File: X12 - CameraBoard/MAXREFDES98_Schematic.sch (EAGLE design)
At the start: 24 parts, among them U1 MB110S-TP, U2 MB110S-TP, U3 MAX5969AETB+, U4 MAX17503ATP+

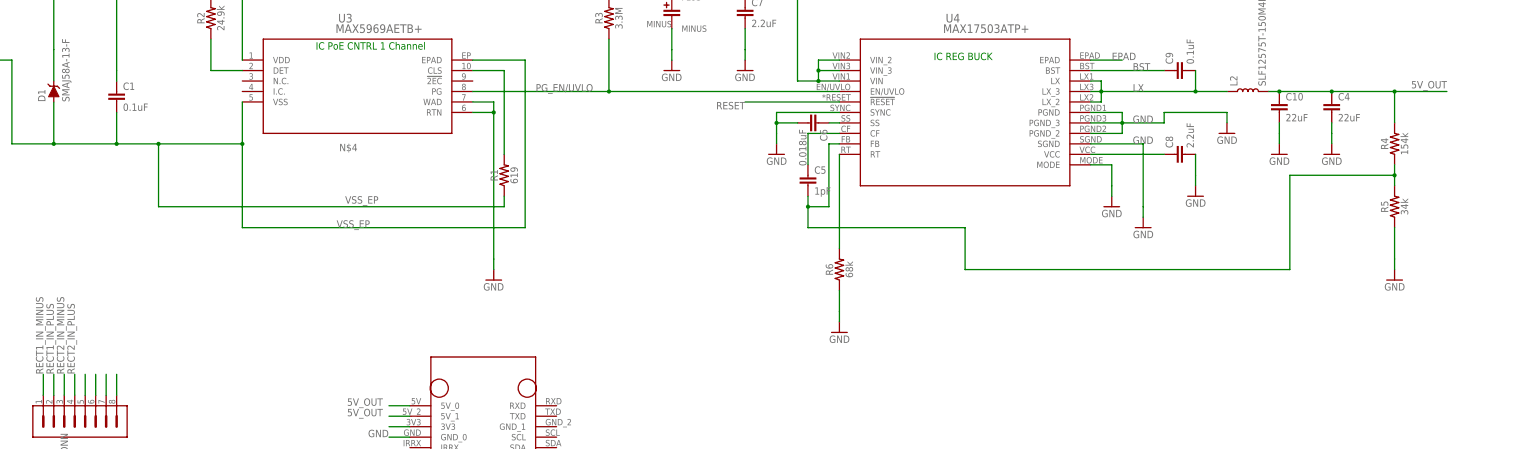
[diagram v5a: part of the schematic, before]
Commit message: Added 0 Ohm Resistor amd 1-pin connector directly to 5V line
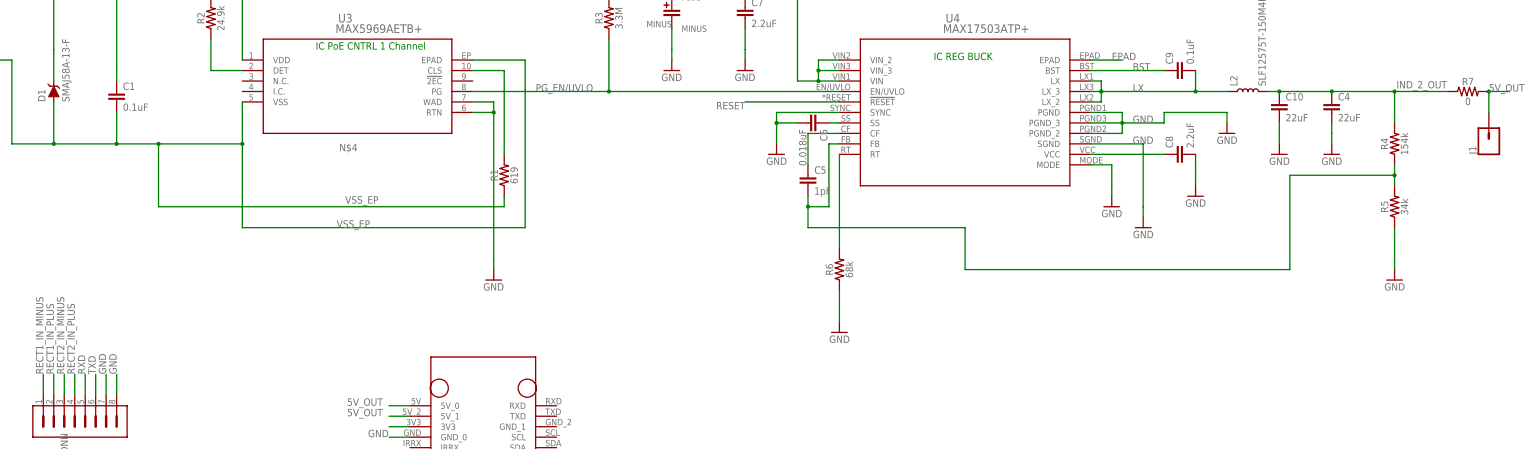
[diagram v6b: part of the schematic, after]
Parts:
- added J1: (no value), SparkFun-Connectors:CONN_01
- added R7: 0, SparkFun-Resistors:0OHM-0603-1/10W-5%
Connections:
- net 5V_OUT5 renamed RXD
- new net IND_2_OUT: C10.1, C4.1, L2.2, R4.2, R7.1
- new net TXD: CONN.6
- net 5V_OUT: now also J1.1, R7.2; no longer C10.1, C4.1, CONN.6, L2.2, R4.2
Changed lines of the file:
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@@
 <part name="CONN" library="Camera_Board_Parts_09_30_2020" deviceset="TERM_BLOCK_PLUG_8POS_STR_2.5MM" device=""/>
 <part name="U$2" library="Camera_Board_Parts_09_30_2020" deviceset="NANO_PI" device=""/>
+<part name="R7" library="SparkFun-Resistors" library_urn="urn:adsk.eagle:library:532" deviceset="0OHM" device="-0603-1/10W-5%" package3d_urn="urn:adsk.eagle:package:39650/1" value="0"/>
+<part name="J1" library="SparkFun-Connectors" library_urn="urn:adsk.eagle:library:513" deviceset="CONN_01" device="" package3d_urn="urn:adsk.eagle:package:38028/1"/>
 </parts>
 <sheets>
@@
 </instance>
 <instance part="U$2" gate="G$1" x="20.32" y="-119.38" smashed="yes"/>
+<instance part="R7" gate="G$1" x="271.78" y="0" smashed="yes">
+<attribute name="NAME" x="271.78" y="1.524" size="1.778" layer="95" font="vector" align="bottom-center"/>
+<attribute name="VALUE" x="271.78" y="-1.524" size="1.778" layer="96" font="vector" align="top-center"/>
+</instance>
+<instance part="J1" gate="G$1" x="276.86" y="-12.7" smashed="yes" rot="R90">
+<attribute name="VALUE" x="281.686" y="-15.24" size="1.778" layer="96" font="vector" rot="R90"/>
+<attribute name="NAME" x="273.812" y="-15.24" size="1.778" layer="95" font="vector" rot="R90"/>
+</instance>
 </instances>
 <busses>
@@
 <net name="5V_OUT" class="0">
 <segment>
-<pinref part="C4" gate="G$1" pin="1"/>
-<pinref part="C10" gate="G$1" pin="1"/>
-<wire x1="226.06" y1="0" x2="238.76" y2="0" width="0.1524" layer="91"/>
-<junction x="226.06" y="0"/>
-<pinref part="L2" gate="G$1" pin="2"/>
-<wire x1="223.52" y1="0" x2="226.06" y2="0" width="0.1524" layer="91"/>
-<pinref part="R4" gate="G$1" pin="2"/>
-<wire x1="238.76" y1="0" x2="254" y2="0" width="0.1524" layer="91"/>
-<wire x1="254" y1="0" x2="254" y2="-7.62" width="0.1524" layer="91"/>
-<junction x="238.76" y="0"/>
-<wire x1="254" y1="0" x2="266.7" y2="0" width="0.1524" layer="91"/>
-<junction x="254" y="0"/>
-<label x="266.7" y="2.54" size="1.778" layer="95" rot="R180"/>
-</segment>
-<segment>
-<pinref part="CONN" gate="G$1" pin="6"/>
-<wire x1="-60.96" y1="-73.66" x2="-60.96" y2="-68.58" width="0.1524" layer="91"/>
-</segment>
-<segment>
 <pinref part="U$2" gate="G$1" pin="5V_0"/>
 <wire x1="15.24" y1="-76.2" x2="10.16" y2="-76.2" width="0.1524" layer="91"/>
@@
 <wire x1="15.24" y1="-78.74" x2="10.16" y2="-78.74" width="0.1524" layer="91"/>
 <label x="0" y="-78.74" size="1.778" layer="95"/>
+</segment>
+<segment>
+<pinref part="R7" gate="G$1" pin="2"/>
+<pinref part="J1" gate="G$1" pin="1"/>
+<wire x1="276.86" y1="0" x2="276.86" y2="-5.08" width="0.1524" layer="91"/>
+<wire x1="276.86" y1="0" x2="281.94" y2="0" width="0.1524" layer="91"/>
+<junction x="276.86" y="0"/>
+<label x="276.86" y="0" size="1.778" layer="95"/>
 </segment>
 </net>
@@
 <pinref part="CONN" gate="G$1" pin="7"/>
 <wire x1="-58.42" y1="-73.66" x2="-58.42" y2="-68.58" width="0.1524" layer="91"/>
+<label x="-58.42" y="-68.58" size="1.778" layer="95" rot="R90"/>
 </segment>
 <segment>
 <pinref part="CONN" gate="G$1" pin="8"/>
 <wire x1="-55.88" y1="-73.66" x2="-55.88" y2="-68.58" width="0.1524" layer="91"/>
+<label x="-55.88" y="-68.58" size="1.778" layer="95" rot="R90"/>
 </segment>
 <segment>
@@
 </segment>
 </net>
-<net name="5V_OUT5" class="0">
+<net name="RXD" class="0">
 <segment>
 <wire x1="-63.5" y1="-73.66" x2="-63.5" y2="-68.58" width="0.1524" layer="91"/>
 <pinref part="CONN" gate="G$1" pin="5"/>
+<label x="-63.5" y="-68.58" size="1.778" layer="95" rot="R90"/>
 </segment>
 </net>
@@
 </segment>
 </net>
+<net name="TXD" class="0">
+<segment>
+<pinref part="CONN" gate="G$1" pin="6"/>
+<wire x1="-60.96" y1="-73.66" x2="-60.96" y2="-68.58" width="0.1524" layer="91"/>
+<label x="-60.96" y="-68.58" size="1.778" layer="95" rot="R90"/>
+</segment>
+</net>
+<net name="IND_2_OUT" class="0">
+<segment>
+<pinref part="C4" gate="G$1" pin="1"/>
+<pinref part="C10" gate="G$1" pin="1"/>
+<wire x1="226.06" y1="0" x2="238.76" y2="0" width="0.1524" layer="91"/>
+<junction x="226.06" y="0"/>
+<pinref part="L2" gate="G$1" pin="2"/>
+<wire x1="223.52" y1="0" x2="226.06" y2="0" width="0.1524" layer="91"/>
+<pinref part="R4" gate="G$1" pin="2"/>
+<wire x1="238.76" y1="0" x2="254" y2="0" width="0.1524" layer="91"/>
+<wire x1="254" y1="0" x2="254" y2="-7.62" width="0.1524" layer="91"/>
+<junction x="238.76" y="0"/>
+<wire x1="254" y1="0" x2="266.7" y2="0" width="0.1524" layer="91"/>
+<junction x="254" y="0"/>
+<label x="266.7" y="2.54" size="1.778" layer="95" rot="R180"/>
+<pinref part="R7" gate="G$1" pin="1"/>
+</segment>
+</net>

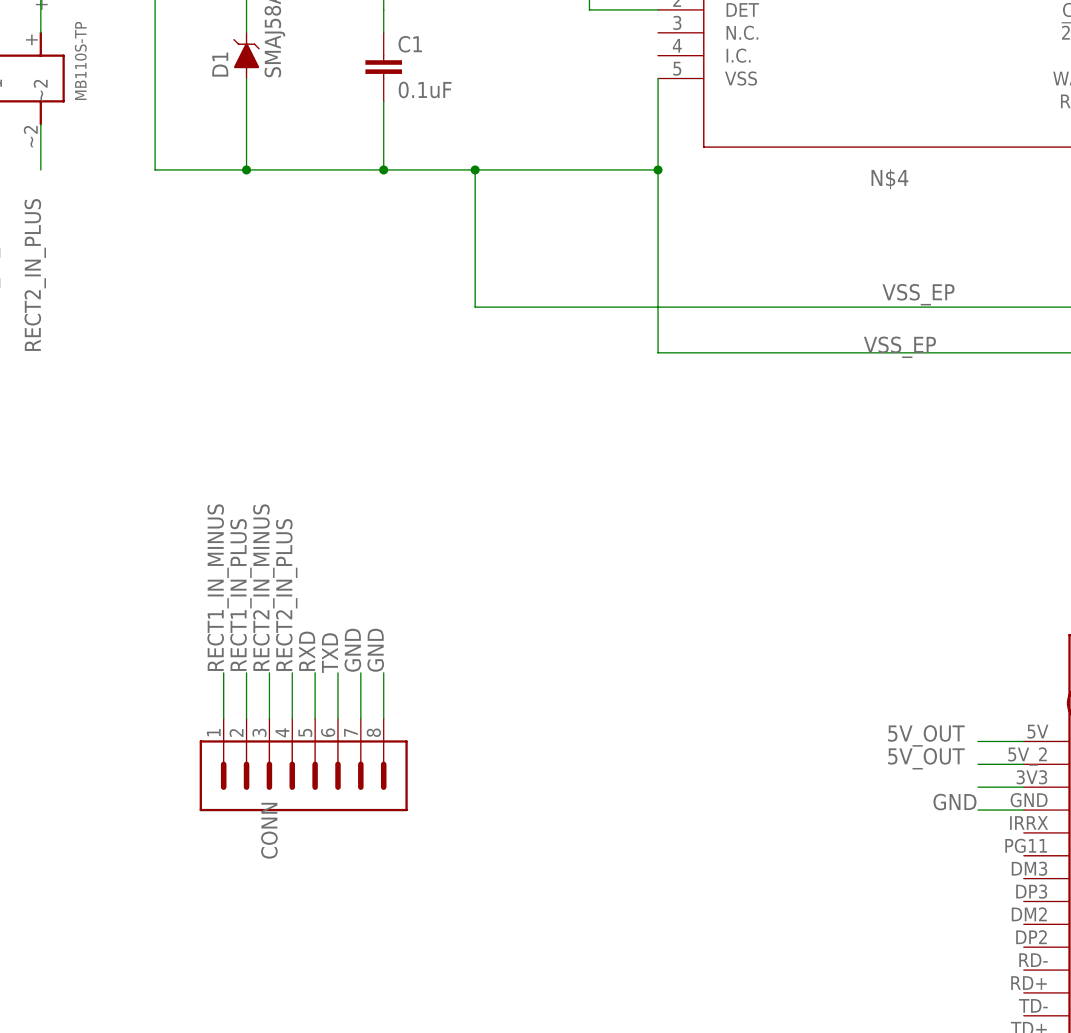
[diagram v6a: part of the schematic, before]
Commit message: Rerouting
Almost done, just need some clarification on the signals connected to the 8-pin connector before I try routing those. If the signals are as I assumed, the 8-pin connector might need to move to the other side of the board.
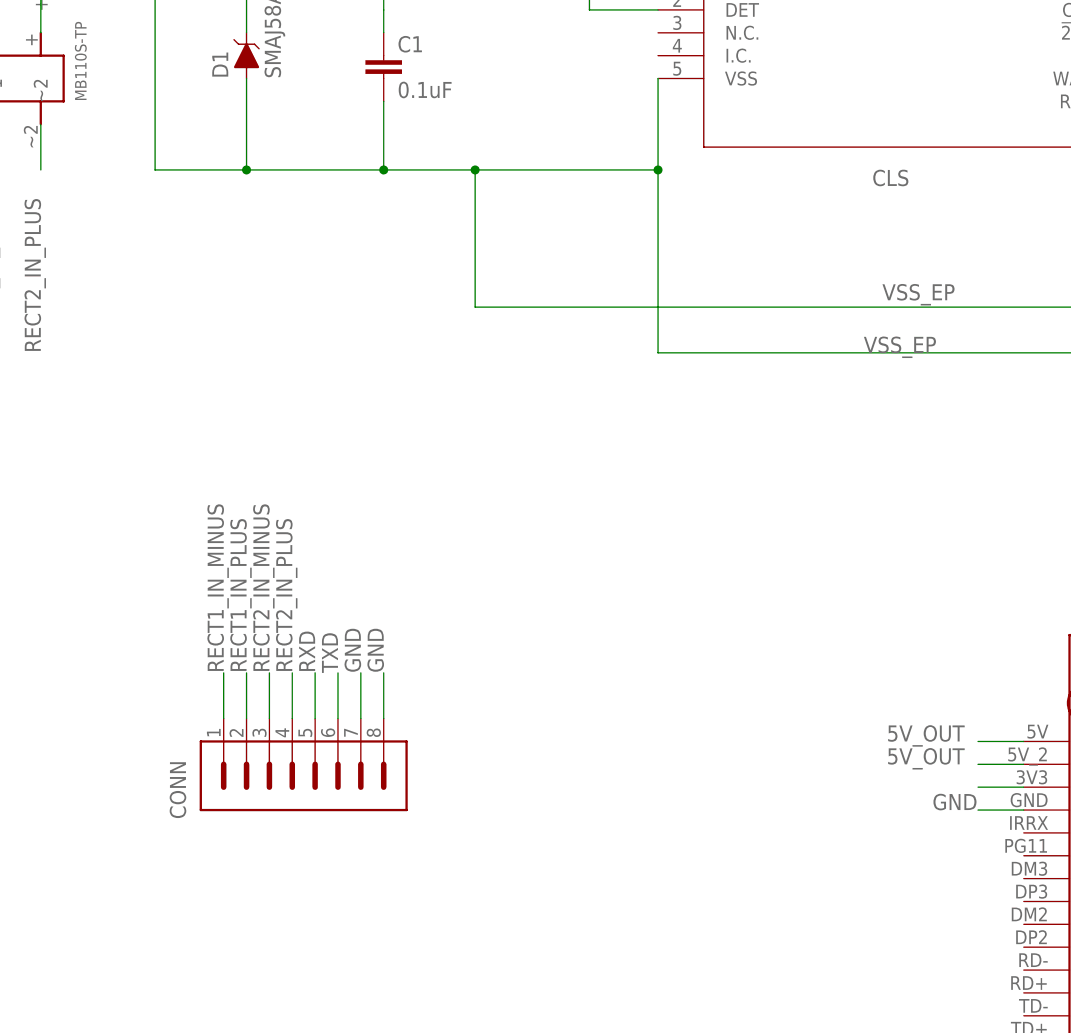
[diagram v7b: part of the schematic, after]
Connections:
- net N$4 renamed CLS
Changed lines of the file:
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@@
 </instance>
 <instance part="CONN" gate="G$1" x="-76.2" y="-76.2" smashed="yes">
-<attribute name="NAME" x="-69.469" y="-82.804" size="1.778" layer="95" rot="R270"/>
+<attribute name="NAME" x="-77.851" y="-84.836" size="1.778" layer="95" rot="R90"/>
 </instance>
 <instance part="U$2" gate="G$1" x="20.32" y="-119.38" smashed="yes"/>
@@
 </segment>
 </net>
-<net name="N$4" class="0">
+<net name="CLS" class="0">
 <segment>
 <pinref part="R1" gate="G$1" pin="2"/>

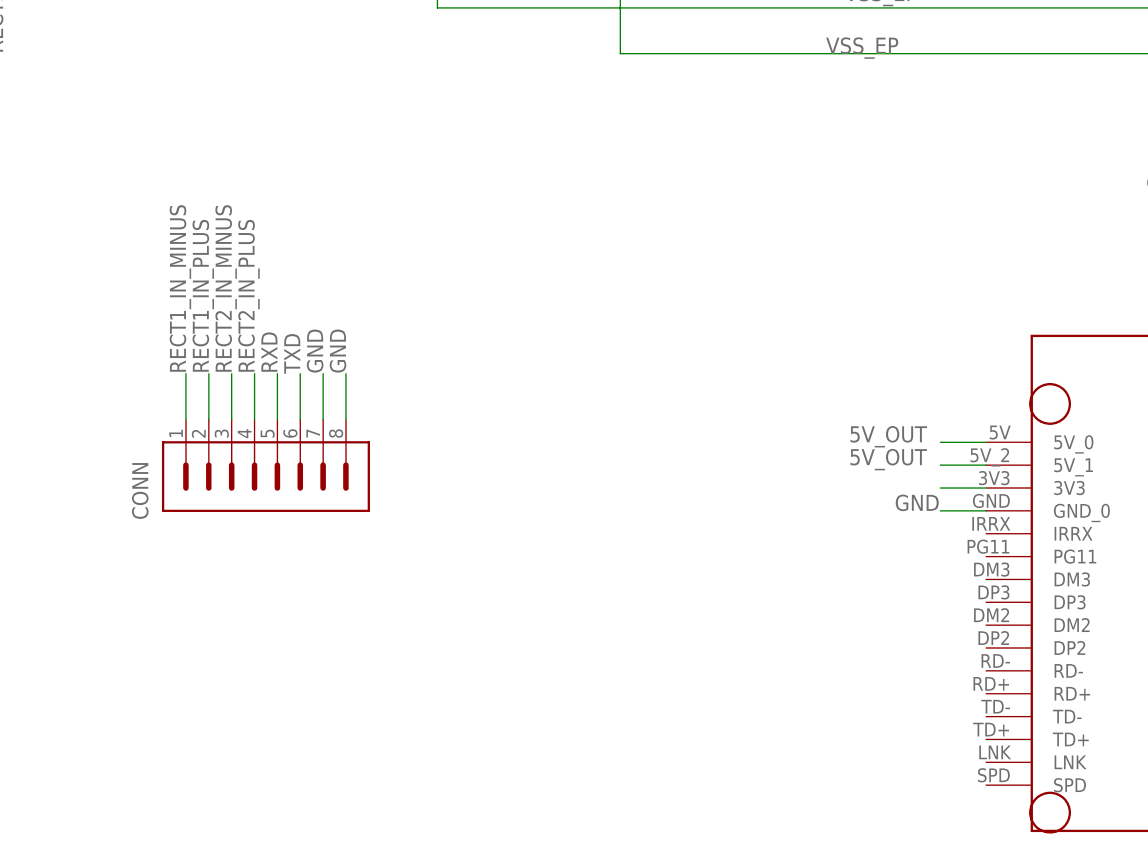
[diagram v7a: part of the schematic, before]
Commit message: Rerouting
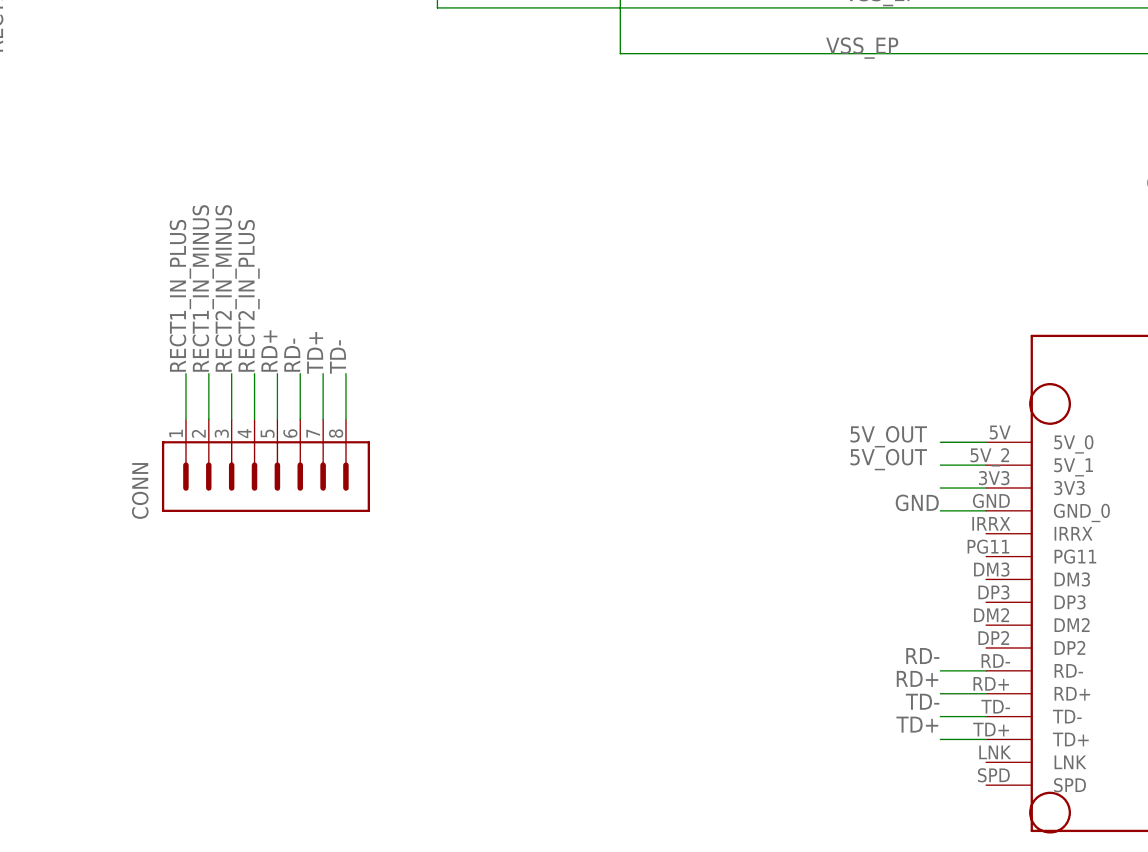
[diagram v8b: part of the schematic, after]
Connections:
- removed net RXD: CONN.5
- removed net TXD: CONN.6
- new net RD+: CONN.5, U$2.RD+
- new net RD-: CONN.6, U$2.RD-
- new net TD+: CONN.7, U$2.TD+
- new net TD-: CONN.8, U$2.TD-
- net GND: no longer CONN.7, CONN.8
- net RECT1_IN_MINUS: now also CONN.2; no longer CONN.1
- net RECT1_IN_PLUS: now also CONN.1; no longer CONN.2
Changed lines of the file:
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@@
-</segment>
-<segment>
-<pinref part="CONN" gate="G$1" pin="7"/>
-<wire x1="-58.42" y1="-73.66" x2="-58.42" y2="-68.58" width="0.1524" layer="91"/>
-<label x="-58.42" y="-68.58" size="1.778" layer="95" rot="R90"/>
-</segment>
-<segment>
-<pinref part="CONN" gate="G$1" pin="8"/>
-<wire x1="-55.88" y1="-73.66" x2="-55.88" y2="-68.58" width="0.1524" layer="91"/>
-<label x="-55.88" y="-68.58" size="1.778" layer="95" rot="R90"/>
 </segment>
 <segment>
@@
 </segment>
 </net>
-<net name="RXD" class="0">
+<net name="RD+" class="0">
 <segment>
 <wire x1="-63.5" y1="-73.66" x2="-63.5" y2="-68.58" width="0.1524" layer="91"/>
 <pinref part="CONN" gate="G$1" pin="5"/>
 <label x="-63.5" y="-68.58" size="1.778" layer="95" rot="R90"/>
+</segment>
+<segment>
+<wire x1="15.24" y1="-104.14" x2="10.16" y2="-104.14" width="0.1524" layer="91"/>
+<pinref part="U$2" gate="G$1" pin="RD+"/>
+<label x="10.16" y="-101.6" size="1.778" layer="95" rot="R180"/>
 </segment>
 </net>
@@
 </segment>
 <segment>
-<wire x1="-73.66" y1="-73.66" x2="-73.66" y2="-68.58" width="0.1524" layer="91"/>
-<pinref part="CONN" gate="G$1" pin="1"/>
-<label x="-73.66" y="-68.58" size="1.778" layer="95" rot="R90"/>
+<pinref part="CONN" gate="G$1" pin="2"/>
+<wire x1="-71.12" y1="-73.66" x2="-71.12" y2="-68.58" width="0.1524" layer="91"/>
+<label x="-71.12" y="-68.58" size="1.778" layer="95" rot="R90"/>
 </segment>
 </net>
@@
 </segment>
 <segment>
-<wire x1="-71.12" y1="-73.66" x2="-71.12" y2="-68.58" width="0.1524" layer="91"/>
-<pinref part="CONN" gate="G$1" pin="2"/>
-<label x="-71.12" y="-68.58" size="1.778" layer="95" rot="R90"/>
+<pinref part="CONN" gate="G$1" pin="1"/>
+<wire x1="-73.66" y1="-73.66" x2="-73.66" y2="-68.58" width="0.1524" layer="91"/>
+<label x="-73.66" y="-68.58" size="1.778" layer="95" rot="R90"/>
 </segment>
 </net>
@@
 </segment>
 <segment>
+<pinref part="CONN" gate="G$1" pin="3"/>
 <wire x1="-68.58" y1="-73.66" x2="-68.58" y2="-68.58" width="0.1524" layer="91"/>
-<pinref part="CONN" gate="G$1" pin="3"/>
 <label x="-68.58" y="-68.58" size="1.778" layer="95" rot="R90"/>
 </segment>
@@
 </segment>
 <segment>
+<pinref part="CONN" gate="G$1" pin="4"/>
 <wire x1="-66.04" y1="-73.66" x2="-66.04" y2="-68.58" width="0.1524" layer="91"/>
-<pinref part="CONN" gate="G$1" pin="4"/>
 <label x="-66.04" y="-68.58" size="1.778" layer="95" rot="R90"/>
 </segment>
 </net>
-<net name="TXD" class="0">
+<net name="RD-" class="0">
 <segment>
 <pinref part="CONN" gate="G$1" pin="6"/>
 <wire x1="-60.96" y1="-73.66" x2="-60.96" y2="-68.58" width="0.1524" layer="91"/>
 <label x="-60.96" y="-68.58" size="1.778" layer="95" rot="R90"/>
+</segment>
+<segment>
+<wire x1="15.24" y1="-101.6" x2="10.16" y2="-101.6" width="0.1524" layer="91"/>
+<pinref part="U$2" gate="G$1" pin="RD-"/>
+<label x="10.16" y="-99.06" size="1.778" layer="95" rot="R180"/>
 </segment>
 </net>
@@
 </segment>
 </net>
+<net name="TD+" class="0">
+<segment>
+<pinref part="CONN" gate="G$1" pin="7"/>
+<wire x1="-58.42" y1="-73.66" x2="-58.42" y2="-68.58" width="0.1524" layer="91"/>
+<label x="-58.42" y="-68.58" size="1.778" layer="95" rot="R90"/>
+</segment>
+<segment>
+<wire x1="15.24" y1="-109.22" x2="10.16" y2="-109.22" width="0.1524" layer="91"/>
+<pinref part="U$2" gate="G$1" pin="TD+"/>
+<label x="10.16" y="-106.68" size="1.778" layer="95" rot="R180"/>
+</segment>
+</net>
+<net name="TD-" class="0">
+<segment>
+<pinref part="CONN" gate="G$1" pin="8"/>
+<wire x1="-55.88" y1="-73.66" x2="-55.88" y2="-68.58" width="0.1524" layer="91"/>
+<label x="-55.88" y="-68.58" size="1.778" layer="95" rot="R90"/>
+</segment>
+<segment>
+<wire x1="15.24" y1="-106.68" x2="10.16" y2="-106.68" width="0.1524" layer="91"/>
+<pinref part="U$2" gate="G$1" pin="TD-"/>
+<label x="10.16" y="-104.14" size="1.778" layer="95" rot="R180"/>
+</segment>
+</net>
